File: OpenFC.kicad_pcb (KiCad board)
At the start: 8 copper layers, 29.5 x 27.6 mm, 173 parts, among them J1 5V, J13 5V, J14 5V, J15 5V, J16 5V, J17 5V, J18 5V, J19 5V, J2 5V, J20 5V, J21 5V, J22 5V, J23 5V, J24 5V, J25 5V, J26 5V, J27 5V, J28 5V, J29 5V, J3 5V, J30 5V, J31 5V, J32 5V, J33 5V, J34 5V, J35 5V, J36 5V, J37 5V, J38 5V, J39 5V, J4 5V, J40 5V, J41 5V, J42 5V, J43 5V, J44 5V, J45 5V, J46 5V, J47 5V, J48 5V, J5 5V, J53 5V, J57 5V, J59 5V, J6 5V, J7 5V, J8 5V, J9 5V, P1 SM08B-SRSS-TB(LF)(SN), Q7 DMN1150UFB-7B, U1 SM06B-SRSS-TB(LF)(SN), U10 TLV75533PDBVR, U11 RP2350A_C42411118, U12 ABM8-272-T3_C20625731, U13 W25Q32RVXHJQ TR, U14 LSM6DSV16XTR, U15 XL-1010RGBC-WS2812B, U16 XL-1010RGBC-WS2812B, U17 XL-1010RGBC-WS2812B, U18 XL-1010RGBC-WS2812B, U19 ESP8285H16, U2 W25Q128JVPIQTR, U20 SX1281IMLTRT, U21 TS2306A 240GF MSM 9_C2976675, U22 XL-1010RGBC-WS2812B, U23 XL-1010RGBC-WS2812B, U24 XL-1010RGBC-WS2812B, U25 XL-1010RGBC-WS2812B, U26 XL-1010RGBC-WS2812B, U27 XL-1010RGBC-WS2812B, U28 XL-1010RGBC-WS2812B, U29 XL-1010RGBC-WS2812B, U3 XL-1010RGBC-WS2812B, U30 BMP388, U4 XL-1010RGBC-WS2812B, U5 XL-1010RGBC-WS2812B, U6 LMR51420YDDCR, U7 LMR51420YDDCR, U8 XL-1010RGBC-WS2812B, U9 TLV75533PDBVR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

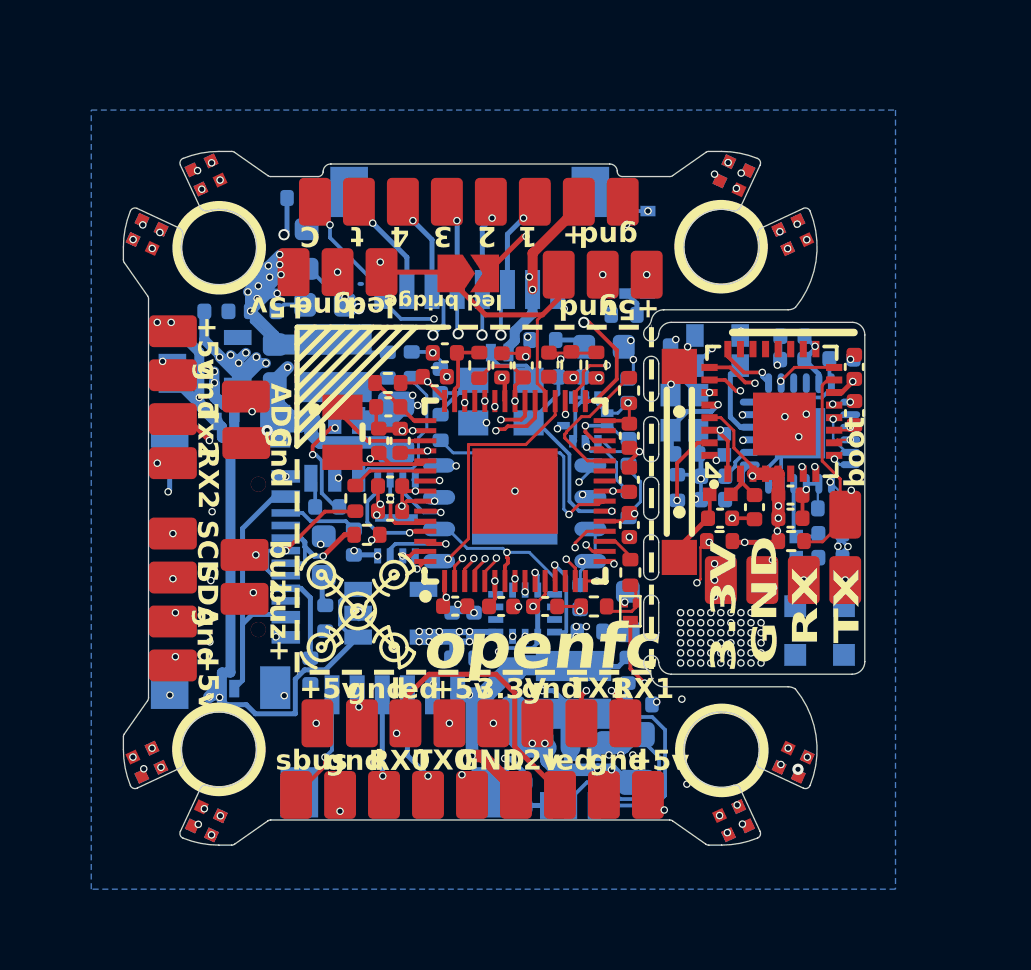
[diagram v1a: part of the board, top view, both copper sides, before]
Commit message: Switched to RP2354A and re-routed
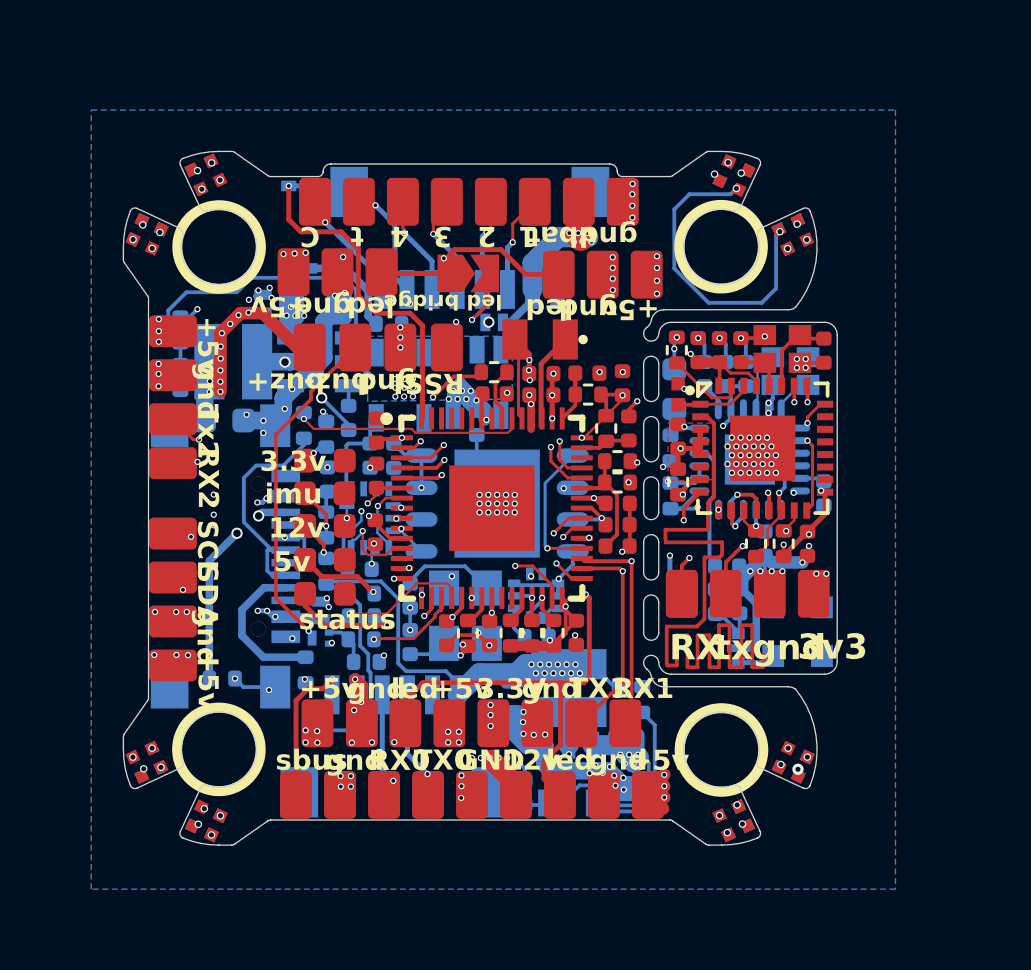
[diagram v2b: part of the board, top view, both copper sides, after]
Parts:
- removed C10, C100, C101, C102, C103, C104, C109, C46, C47, C48, C97, C98, C99: 100n, Capacitor_SMD:C_0402_1005Metric
- removed C105, C106: 15p, Capacitor_SMD:C_0402_1005Metric
- removed C43, C44, C45: 4.7uF, Capacitor_SMD:C_0402_1005Metric
- removed D2: LED_1_Green, LED_SMD:LED_0603_1608Metric
- removed J57: 5V, lib:small_pad
- removed L13: ANT8010LL04R2400A, lib:ANT-SMD_L8.0-W1.0-SLDA81-3R010G-S1TF
- removed L7, L9: LQW15AN3N0B00D (3nH), lib:L0402
- removed OSC1: OW7EL89CENUNFAYLC-52M, lib:OSC-SMD_4P-L2.0-W1.6-BL_TXC_7Z
- removed R1, R2: 5.1k, Resistor_SMD:R_0402_1005Metric
- removed R10, R12: 10k, Resistor_SMD:R_0402_1005Metric
- removed R39: 33R, Resistor_SMD:R_0402_1005Metric
- removed R41: 200R, Resistor_SMD:R_0402_1005Metric
- removed R42: 1k, Resistor_SMD:R_0402_1005Metric
- removed R46, R47: 22R, Resistor_SMD:R_0402_1005Metric
- removed R53: 30R, Resistor_SMD:R_0402_1005Metric
- removed U11: RP2350A_C42411118, lib:QFN-60_L7.0-W7.0-P0.40-TL-EP3.4
- removed U12: ABM8-272-T3_C20625731, lib:CRYSTAL-SMD_4P-L3.2-W2.5-BL
- removed U13: W25Q32RVXHJQ TR, lib:USON-8_L3.0-W2.0-P0.50-BL-EP
- removed U21: TS2306A 240GF MSM 9_C2976675, lib:SW-SMD_4P-L3.0-W2.0-P0.85-LS3.5
- added C21: 4.7uF, Capacitor_SMD:C_0402_1005Metric, F.Cu at (65.9, 106.5)
- added C22: 4.7uF, Capacitor_SMD:C_0402_1005Metric, F.Cu at (67.7, 106.5)
- added C23: 4.7uF, Capacitor_SMD:C_0402_1005Metric, F.Cu at (69.4, 108.7)
- added C24: 100n, Capacitor_SMD:C_0402_1005Metric, F.Cu at (76.5, 113.3)
- added C25: 100n, Capacitor_SMD:C_0402_1005Metric, F.Cu at (68.9, 112.5)
- added C26: 100n, Capacitor_SMD:C_0402_1005Metric, F.Cu at (69.1, 106.9)
- added C27: 100n, Capacitor_SMD:C_0402_1005Metric, F.Cu at (64.0, 107.3)
- added C28: 100n, Capacitor_SMD:C_0402_1005Metric, F.Cu at (67.3, 116.8)
- added C29: 100n, Capacitor_SMD:C_0402_1005Metric, F.Cu at (59.3, 112.8)
- added C30: 100n, Capacitor_SMD:C_0402_1005Metric, F.Cu at (62.1, 116.8)
- added C31: 100n, Capacitor_SMD:C_0402_1005Metric, F.Cu at (59.4, 108.8)
- added C32: 15p, Capacitor_SMD:C_0402_1005Metric, B.Cu at (60.7, 117.2)
- added C33: 15p, Capacitor_SMD:C_0402_1005Metric, B.Cu at (60.7, 115.3)
- added C34: 100n, Capacitor_SMD:C_0402_1005Metric, B.Cu at (58.7, 114.3)
- added C6: 4.7uF, Capacitor_SMD:C_0402_1005Metric, F.Cu at (65.9, 107.3)
- added D6: LED_1_Green, LED_SMD:LED_0603_1608Metric, F.Cu at (57.3, 115.2)
- added D7: LED, LED_SMD:LED_0603_1608Metric, B.Cu at (71.2, 107.1)
- added FL1: 2450FM07D0034T, lib:FILTER-SMD_4P-L1.0-W0.5-L, B.Cu at (73.8, 117.4)
- added J56: 5V, lib:small_pad, F.Cu at (62.1, 105.5)
- added L2: AOTA-B201610S3R3-101-T, lib:IND-SMD_L2.0-W1.6_AOTA-B201610S3R3-101-T, F.Cu at (65.9, 105.1)
- added R17: 22R, Resistor_SMD:R_0402_1005Metric, B.Cu at (56.5, 108.5)
- added R18: 22R, Resistor_SMD:R_0402_1005Metric, F.Cu at (64.0, 106.4)
- added R19: 33R, Resistor_SMD:R_0402_1005Metric, F.Cu at (67.8, 107.3)
- added R20: 200R, Resistor_SMD:R_0402_1005Metric, F.Cu at (68.5, 108.7)
- added R21: 1k, Resistor_SMD:R_0402_1005Metric, F.Cu at (63.0, 116.8)
- added R22: 30R, Resistor_SMD:R_0402_1005Metric, B.Cu at (58.8, 116.1)
- added R23: 5.1k, Resistor_SMD:R_0402_1005Metric, F.Cu at (65.5, 116.8)
- added R24: 5.1k, Resistor_SMD:R_0402_1005Metric, F.Cu at (66.4, 116.8)
- added R25: 10k, Resistor_SMD:R_0402_1005Metric, F.Cu at (64.7, 116.8)
- added R26: 10k, Resistor_SMD:R_0402_1005Metric, B.Cu at (59.8, 104.5)
- added R33: 3.3k, Resistor_SMD:R_0402_1005Metric, B.Cu at (71.0, 109.5)
- added R35: 10k, Resistor_SMD:R_0402_1005Metric, F.Cu at (74.5, 113.3)
- added U32: RP2354A, lib:QFN-60_L7.0-W7.0-P0.40-TL-EP3.4, F.Cu at (63.9, 111.8)
- added U33: ABM8-272-T3_C20625731, lib:CRYSTAL-SMD_4P-L3.2-W2.5-BL, B.Cu at (62.9, 116.1)
- added U34: TS2306A 240GF MSM 9_C2976675, lib:SW-SMD_4P-L3.0-W2.0-P0.85-LS3.5, B.Cu at (56.3, 100.7)
- added X2: Q22FA12800519, lib:CRYSTAL-SMD_4P-L2.0-W1.6-BL, B.Cu at (75.8, 106.4)
- C13, C18, C19, D1, D3, D4, D5, L8, R7, X1: moved to F.Cu
- C14, C8, J59, Q7, R13, R5: moved to B.Cu
- C15: value 1.2p -> 100n
- C20: value 1.2p -> 100n; moved to F.Cu
- C42: value 4.7uF -> 100n
- L1: value AOTA-B201610S3R3-101-T -> 3n; footprint lib:IND-SMD_L2.0-W1.6_AOTA-B201610S3R3-101-T -> Inductor_SMD:L_0402_1005Metric; moved to B.Cu
- moved L1 16.3 mm to (72.8, 115.5), turned to -90 degrees
- moved C20 13.9 mm to (63.9, 116.8), turned to -90 degrees
- moved C15 13.8 mm to (59.4, 110.5), turned to 90 degrees
- moved D4 12.9 mm to (57.3, 111.2), turned to 180 degrees
- moved Q7 12.4 mm to (57.1, 117.0), turned to 0 degrees
- moved R15 11.9 mm to (58.8, 115.2)
- moved R4 11.3 mm to (57.4, 112.5), turned to -90 degrees
- moved C3 11.3 mm to (63.3, 108.5), turned to -90 degrees
- moved R13 11.0 mm to (58.7, 117.1), turned to 180 degrees
- moved U9 10.9 mm to (63.4, 106.8), turned to 90 degrees
- moved C111 10.4 mm to (65.7, 117.0), turned to 180 degrees
- moved J39 10.3 mm to (56.7, 105.5), turned to 90 degrees
- moved D1 10.2 mm to (57.3, 113.9)
- moved C42 9.83 mm to (69.0, 111.7), turned to 0 degrees
- moved R3 9.46 mm to (57.4, 108.9), turned to -90 degrees
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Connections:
- net /RP2350A/VBAT_ADC renamed Net-(U32-GPIO26_ADC0)
- AE1 pad 3: Net-(AE1-Pad3) -> Net-(FL1-OUT)
- C14 pad 1: Net-(U19-LNA) -> Net-(U20-RFIO)
- C15 pad 1: Net-(C15-Pad1) -> +1.1V
- C17 pad 1: Net-(U20-RFIO) -> Net-(FL1-IN)
- C20 pad 1: Net-(AE1-Pad3) -> +1.1V
- L1 pad 1: +1.1V -> Net-(U20-RFIO)
- L1 pad 2: Net-(U11-VREG_LX) -> Net-(FL1-IN)
- U14 pad 2: unconnected-(U14-SDx/AH1/Qvar1-Pad2) -> GND
- U14 pad 3: unconnected-(U14-SCx/AH2/Qvar2-Pad3) -> GND
- U19 pad 14: +3.3V -> /ELRS/RST
- U19 pad 2: Net-(U19-LNA) -> /ELRS/ANT_TRACE
- U19 pad 8: /ELRS/RST -> Net-(U19-XDP_DCDC)
- U20 pad 4: /ELRS/RADIO_OSC -> Net-(U20-XTA)
- U20 pad 6: unconnected-(U20-XTB-Pad6) -> Net-(U20-XTB)
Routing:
- net +4.5V: track 135.7 -> 36.6 mm, vias 11 -> 28
- net /ELRS/ANT_TRACE: track 0.00 -> 32.7 mm
- net Net-(U11-QSPI_SS): track 30.0 -> 0.00 mm, vias 2 -> 0
- net +3.3V: track 80.7 -> 56.0 mm
- net GND: track 82.1 -> 65.2 mm, vias 138 -> 154
- net /PADS/BUZZER-: track 29.2 -> 13.5 mm, vias 2 -> 1
- net Net-(U32-QSPI_SS): track 0.00 -> 14.0 mm, vias 0 -> 1
- net /PADS/SBUS: track 4.57 -> 17.5 mm, vias 1 -> 2
- net /ELRS/ESP_BOOT0: track 33.0 -> 20.6 mm, vias 2 -> 3
- net /PADS/CURRENT: track 10.5 -> 22.1 mm, vias 3 -> 2
- net +5V: track 38.0 -> 27.3 mm, vias 20 -> 35
- net /PADS/ADC1: track 9.96 -> 0.00 mm, vias 2 -> 0
- net Net-(U11-XOUT): track 9.20 -> 0.00 mm, vias 1 -> 0
- net Net-(U32-USB_DM): track 0.00 -> 8.99 mm, vias 0 -> 1
- net /PADS/ADC2: track 0.00 -> 8.64 mm, vias 0 -> 2
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- added copper zone on F.Cu, net +3.3V
- added copper zone on B.Cu, net +4.5V
- added copper zone on In5.Cu, net +4.5V
- removed copper zone on In4.Cu, net +3.3V_GYRO
- removed copper zone on In5.Cu, net GND
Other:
- board size 29.5 x 27.6 mm -> 28.4 x 27.6 mm
- board text added: "3.3v"
- board text added: "3v3"
- board text added: "5v"
- board text added: "RSSI"
- board text added: "imu"
- board text added: "tx"
- board text added: "vbat"
- board text removed: "+"
- board text removed: "+12v"
- board text removed: "+3.3 imu"
- board text removed: "+3.3v"
- board text removed: "ADC"
- board text removed: "EXPRESSLRS"
- board text removed: "TX"
- board text removed: "break me"
- board text removed: "receiver"

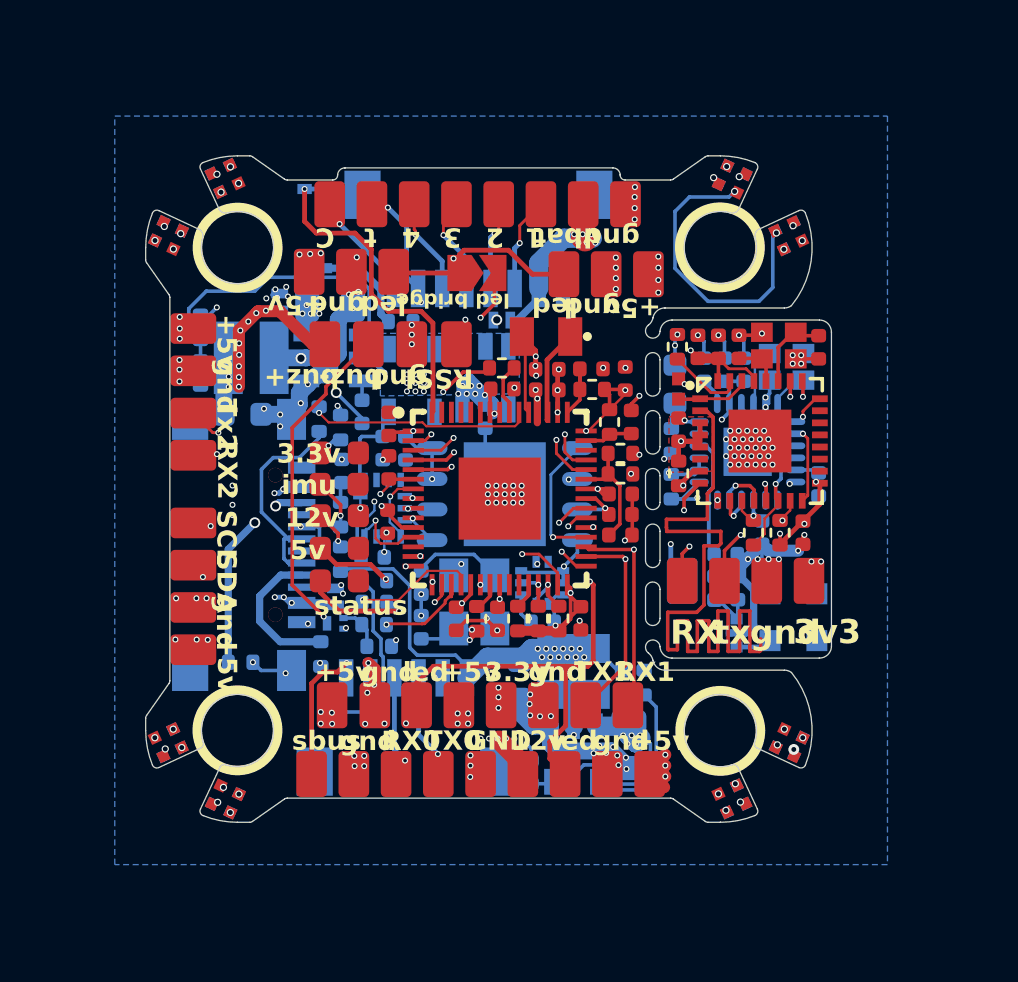
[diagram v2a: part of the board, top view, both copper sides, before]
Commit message: Added Open-OSD-X and new layout
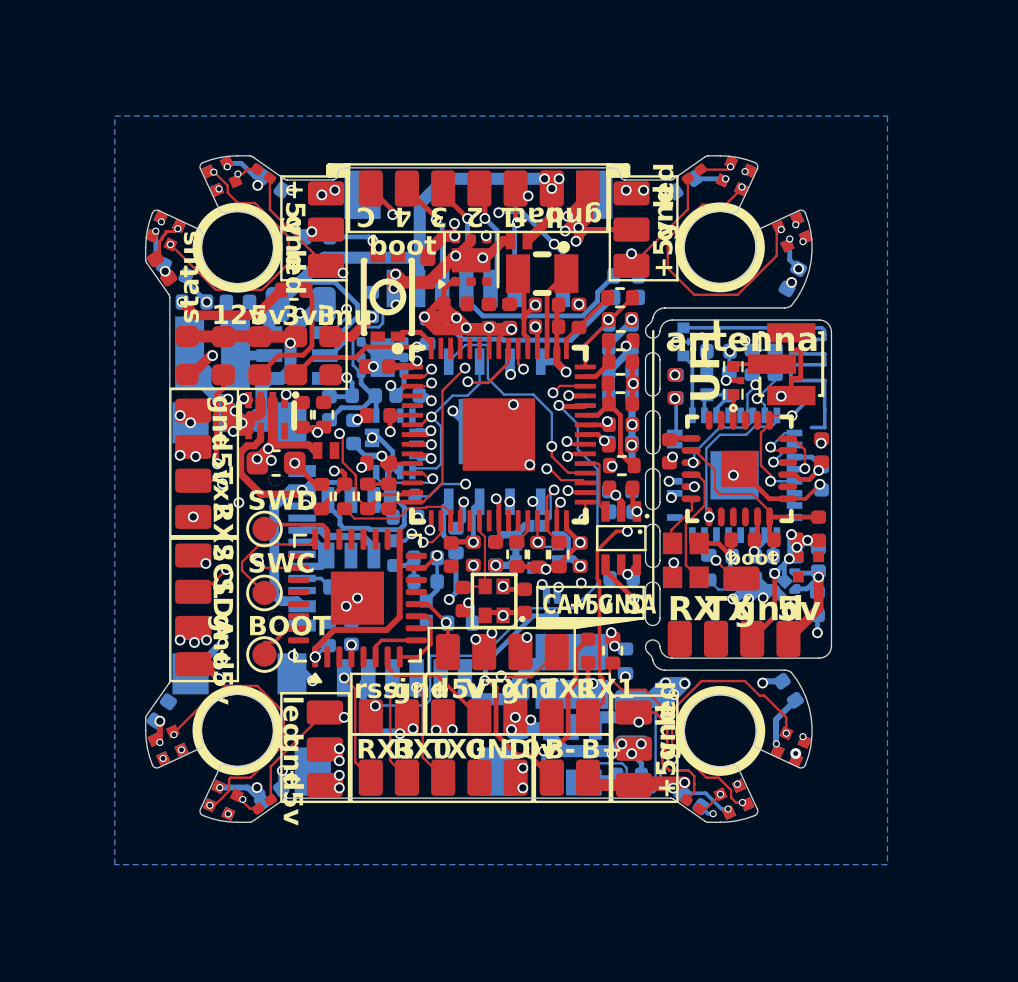
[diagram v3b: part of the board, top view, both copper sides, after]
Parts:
- removed AE1: 47948-0001, lib:ANT-SMD_47948-0001
- removed C110: 100n, Capacitor_SMD:C_0402_1005Metric
- removed D20, D23: RB161QS-40_C28646385, lib:SOD-882_L1.0-W0.6-RD
- removed D7: LED, LED_SMD:LED_0603_1608Metric
- removed J37, J41, J59: 5V, lib:small_pad
- removed L8: BLM15PD121SN1D, lib:L0402
- removed R33: 3.3k, Resistor_SMD:R_0402_1005Metric
- removed R35: 10k, Resistor_SMD:R_0402_1005Metric
- removed X1: XTM20026000FT00351005, lib:CRYSTAL-SMD_4P-L2.0-W1.6-BL
- added C10: 100n, Capacitor_SMD:C_0402_1005Metric, F.Cu at (65.0, 116.1)
- added C16: 22uF, Capacitor_SMD:C_0402_1005Metric, F.Cu at (62.1, 103.8)
- added C43: 22uF, Capacitor_SMD:C_0402_1005Metric, B.Cu at (56.9, 108.1)
- added C44: 100n, Capacitor_SMD:C_0402_1005Metric, B.Cu at (69.0, 115.2)
- added C45: 100n, Capacitor_SMD:C_0402_1005Metric, F.Cu at (61.9, 114.2)
- added C46: 100n, Capacitor_SMD:C_0402_1005Metric, B.Cu at (54.5, 124.1)
- added C47: 100n, Capacitor_SMD:C_0402_1005Metric, B.Cu at (50.0, 120.7)
- added C48: 22uF, Capacitor_SMD:C_0603_1608Metric, F.Cu at (54.7, 110.4)
- added C49: 100n, Capacitor_SMD:C_0402_1005Metric, B.Cu at (68.9, 111.5)
- added C50: 100n, Capacitor_SMD:C_0402_1005Metric, B.Cu at (73.5, 107.1)
- added C51: 100n, Capacitor_SMD:C_0402_1005Metric, B.Cu at (73.0, 105.7)
- added C52: 100n, Capacitor_SMD:C_0402_1005Metric, B.Cu at (71.2, 107.2)
- added C53: 100n, Capacitor_SMD:C_0402_1005Metric, B.Cu at (74.0, 114.2)
- added C54: 100n, Capacitor_SMD:C_0402_1005Metric, B.Cu at (77.3, 111.0)
- added C55: 100n, Capacitor_SMD:C_0402_1005Metric, B.Cu at (75.8, 114.2)
- added C56: 100n, Capacitor_SMD:C_0402_1005Metric, F.Cu at (71.2, 107.2)
- added C57: 100n, Capacitor_SMD:C_0402_1005Metric, B.Cu at (75.9, 119.8)
- added C58: 100n, Capacitor_SMD:C_0402_1005Metric, B.Cu at (71.9, 124.3)
- added C59: 100n, Capacitor_SMD:C_0402_1005Metric, B.Cu at (68.9, 109.5)
- added C60: 100n, Capacitor_SMD:C_0402_1005Metric, B.Cu at (68.9, 107.6)
- added C61: 100n, Capacitor_SMD:C_0402_1005Metric, B.Cu at (68.9, 105.6)
- added C64: 100n, Capacitor_SMD:C_0402_1005Metric, B.Cu at (68.9, 106.6)
- added C65: 100n, Capacitor_SMD:C_0402_1005Metric, B.Cu at (68.9, 104.6)
- added C66: 100n, Capacitor_SMD:C_0402_1005Metric, B.Cu at (69.0, 112.4)
- added C69: 100n, Capacitor_SMD:C_0402_1005Metric, B.Cu at (60.9, 114.3)
- added C71: 100n, Capacitor_SMD:C_0402_1005Metric, B.Cu at (60.9, 115.3)
- added C75: 100n, Capacitor_SMD:C_0402_1005Metric, B.Cu at (56.9, 117.5)
- added C76: 100n, Capacitor_SMD:C_0402_1005Metric, B.Cu at (57.8, 117.4)
- added D2: USBLC6-2SC6, lib:SOT-23-6_L2.9-W1.6-P0.95-LS2.8-BL, B.Cu at (57.8, 113.0)
- added D8: LED_1_Green, LED_SMD:LED_0603_1608Metric, F.Cu at (56.9, 105.9)
- added FL2: 2450FM07D0034T, lib:FILTER-SMD_4P-L1.0-W0.5-L, B.Cu at (71.5, 105.3)
- added J10: 5V, lib:small_pad, F.Cu at (72.9, 117.7)
- added J11: 5V, lib:small_pad, F.Cu at (71.4, 117.7)
- added J12: 5V, lib:small_pad, F.Cu at (74.0, 115.2)
- added J49: 5V, lib:small_pad, F.Cu at (63.3, 118.2)
- added J50: 5V, lib:small_pad, F.Cu at (64.8, 118.2)
- added JP2: SolderJumper_2_Open, Panelization:MouseBite-Slot-Jumper_0201, F.Cu at (71.9, 124.5)
- added JP3: SolderJumper_2_Open, Panelization:MouseBite-Slot-Jumper_0201, F.Cu at (54.2, 98.4)
- added JP4: SolderJumper_2_Open, Panelization:MouseBite-Slot-Jumper_0201, F.Cu at (72.0, 98.4)
- added L7: LQG15HS2N0S02D, lib:L0402, B.Cu at (72.5, 107.1)
- added R1: 10k, Resistor_SMD:R_0402_1005Metric, B.Cu at (72.6, 114.7)
- added R10: 6.8k, Resistor_SMD:R_0402_1005Metric, F.Cu at (59.4, 111.8)
- added R2: 75, Resistor_SMD:R_0402_1005Metric, B.Cu at (62.3, 117.0)
- added R34: 6.8k, Resistor_SMD:R_0402_1005Metric, F.Cu at (58.5, 111.8)
- added R36: 6.8k, Resistor_SMD:R_0402_1005Metric, B.Cu at (69.2, 102.6)
- added R37: 6.8k, Resistor_SMD:R_0402_1005Metric, B.Cu at (69.2, 103.5)
- added RF1: CONUFL001-SMD-T, lib:IPEX-SMD_3P-L2.6-W2.6-LS3.0, F.Cu at (75.6, 106.3)
- added TP1: TestPoint, TestPoint:TestPoint_Pad_D1.0mm, F.Cu at (54.2, 113.1)
- added TP2: TestPoint, TestPoint:TestPoint_Pad_D1.0mm, F.Cu at (54.2, 115.8)
- added TP3: TestPoint, TestPoint:TestPoint_Pad_D1.0mm, F.Cu at (54.2, 118.3)
- added U12: WL9005D4-33, lib:UDFN-4_L1.0-W1.0-P0.65-TL, B.Cu at (75.8, 115.3)
- added U13: TPS746-3.3DRV, Package_SON:WSON-6-1EP_2x2mm_P0.65mm_EP1x1.6mm, F.Cu at (62.8, 102.0)
- added U21: TPS746-3.3DRV, Package_SON:WSON-6-1EP_2x2mm_P0.65mm_EP1x1.6mm, B.Cu at (59.1, 106.0)
- added U35: STM32G431KBUx, Package_DFN_QFN:QFN-32-1EP_5x5mm_P0.5mm_EP3.1x3.1mm, F.Cu at (58.0, 116.0)
- added X3: OT4EL89CJI-111YLC-12M, lib:OSC-SMD_4P-L1.6-W1.2-BL-1, F.Cu at (63.7, 116.1)
- C1, C36, C5, C7, C8, C9, D21, FL1, R13, R14, R15, R5, U20, U34, X2: moved to F.Cu
- C11, C12, C13, R18, R6: moved to B.Cu
- C14: value 1.2p -> 100n
- C17: value 1.2p -> 22uF
- C18: value 15p -> 100n; moved to B.Cu
- C19, C33: value 15p -> 100n
- C3: value 22uF -> 15p; moved to F.Cu
- C32: value 15p -> 100n; moved to F.Cu
- C4: value 22uF -> 100n; moved to F.Cu
- D3: value LED_1_Green -> RB161QS-40_C28646385; footprint LED_SMD:LED_0603_1608Metric -> lib:SOD-882_L1.0-W0.6-RD
- JP1: footprint Jumper:SolderJumper-2_P1.3mm_Open_TrianglePad1.0x1.5mm -> Panelization:MouseBite-Slot-Jumper_0201
- L1: value 3n -> BLM15AG601SN1D; footprint Inductor_SMD:L_0402_1005Metric -> lib:L0402
- R21: value 1k -> 33R; moved to B.Cu
- R3: value 33R -> 10k
- R7: value 12k -> 100k
- R8: value 10k -> 39k
- U10: value TLV75533PDBVR -> GD25Q256EWIGR; footprint lib:SOT-23-5_L3.0-W1.7-P0.95-LS2.8-BR -> lib:WSON-8_L6.0-W5.0-P1.27-TL-EP
- U19: value ESP8285H16 -> XL-1010RGBC-WS2812B; footprint lib:QFN-32_L5.0-W5.0-P0.50-TL-EP3.7 -> lib:LED-SMD_4P-L1.0-W1.0-TL_XL-1010RGBC-WS2812B
- U2: value W25Q128JVPIQTR -> ESP32-C3FH4; footprint lib:WSON-8_L6.0-W5.0-P1.27-BL-EP -> lib:QFN-32_L5.0-W5.0-P0.50-TL-EP3.7
- U33: value ABM8-272-T3_C20625731 -> TPS2116DRLR; footprint lib:CRYSTAL-SMD_4P-L3.2-W2.5-BL -> lib:SOT-583-8_L2.1-W1.6-P0.50-LS1.6-BL; moved to F.Cu
- U9: value TLV75533PDBVR -> TXU0101DCKR; footprint lib:SOT-23-5_L3.0-W1.7-P0.95-LS2.8-BR -> lib:SC-70-6_L2.0-W1.3-P0.65-LS2.1-BL; moved to F.Cu
- moved J26 24.9 mm to (75.9, 117.7)
- moved C19 24.1 mm to (50.0, 102.3), turned to -55 degrees
- moved JP1 23.7 mm to (54.2, 124.5), turned to -55 degrees
- moved C18 23.6 mm to (54.5, 98.8), turned to -35 degrees
- moved J39 21.0 mm to (67.6, 123.4)
- moved R8 19.5 mm to (56.6, 108.4)
- moved J40 19.5 mm to (66.1, 123.4)
- moved R3 18.2 mm to (75.3, 106.2)
- moved J56 15.9 mm to (58.6, 120.9)
- moved R7 15.8 mm to (55.8, 108.4), turned to -90 degrees
- moved J9 15.5 mm to (60.1, 120.9)
- moved C32 14.8 mm to (61.0, 102.4)
- moved R21 13.7 mm to (58.6, 103.8), turned to -90 degrees
- moved C28 12.9 mm to (64.3, 104.3), turned to 90 degrees
- moved R29 12.5 mm to (69.2, 118.6), turned to -90 degrees
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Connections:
- net /PADS/M1 renamed /RP2350A/Motor1
- net /PADS/M2 renamed /RP2350A/Motor2
- net /PADS/M3 renamed /RP2350A/Motor3
- net /PADS/M4 renamed /RP2350A/Motor4
- C11 pad 1: +3.3V -> +5V
- C12 pad 1: +3.3V -> +5V
- C13 pad 1: +3.3V -> +5V
- C14 pad 1: Net-(U20-RFIO) -> +5V
- C17 pad 1: Net-(FL1-IN) -> +3.3V_ELRS
- C18 pad 1: GND -> +5V
- C18 pad 2: Net-(U19-XTAL_OUT) -> GND
- C19 pad 1: GND -> +5V
- C19 pad 2: Net-(U19-XTAL_IN) -> GND
- C3 pad 1: +3.3V -> GND
- C3 pad 2: GND -> /RP2350A/Xin
- C32 pad 1: GND -> +5V
- C32 pad 2: Net-(C32-Pad2) -> GND
- C33 pad 1: /RP2350A/Xin -> +5V
- C4 pad 1: +3.3V_GYRO -> +3.3V
- C40 pad 1: +5V -> +5V_BUCK
- C5 pad 1: +3.3V -> +3.3V_ELRS
- C8 pad 1: +3.3V -> +3.3V_ELRS
- D3 pad 1: GND -> +5V
- D3 pad 2: Net-(D3-A) -> +5V_BUCK
- J26 pad 1: /PADS/ESC_TELEM -> +5V
- J31 pad 1: +3.3V -> GND
- J32 pad 1: /UART1_RX -> /OSD/VIDEO_IN
- J33 pad 1: /UART1_TX -> /OSD/VIDEO_OUT
- J34 pad 1: GND -> /OSD/SA_OUT
- L1 pad 1: Net-(U20-RFIO) -> +3.3V
- L1 pad 2: Net-(FL1-IN) -> Net-(U35-VDDA)
- L4 pad 2: +5V -> +5V_BUCK
- P1 pad 1: /PADS/CURRENT -> GND
- P1 pad 2: /PADS/ESC_TELEM -> +BATT
- P1 pad 8: GND -> /PADS/CURRENT
- R15 pad 1: +5V -> +5V_BUCK
- R16 pad 2: +5V -> +5V_BUCK
- R21 pad 1: Net-(C32-Pad2) -> +3.3V_GYRO
- R21 pad 2: /RP2350A/Xout -> Net-(D8-A)
- R3 pad 1: +3.3V -> +3.3V_ELRS
- R3 pad 2: Net-(D3-A) -> /ELRS/ESP8285_EN
- R4 pad 1: +3.3V_GYRO -> +3.3V
- R6 pad 1: +3.3V -> +3.3V_ELRS
- R6 pad 2: /ELRS/ESP8285_EN -> /ELRS/RST
- R7 pad 1: Net-(U19-RES12K) -> +5V_BUCK
- R7 pad 2: GND -> Net-(U33-PR1)
- R8 pad 1: +3.3V -> Net-(U33-PR1)
- R8 pad 2: /ELRS/ESP_BOOT0 -> GND
- U10 pad 1: +4.5V -> /BLACKBOX/BB_CS
- U10 pad 2: GND -> /BLACKBOX/SPI.MISO
- U10 pad 3: +4.5V -> +3.3V
- U10 pad 4: unconnected-(U10-NC-Pad4) -> GND
- U10 pad 5: +3.3V_GYRO -> /BLACKBOX/SPI.MOSI
- U15 pad 2: +4.5V -> +5V
- U15 pad 4: Net-(U15-DIN) -> Net-(JP1-B)
- U16 pad 2: +4.5V -> +5V
- U17 pad 2: +4.5V -> +5V
- U17 pad 4: Net-(U16-DOUT) -> Net-(JP2-B)
- U18 pad 2: +4.5V -> +5V
- U19 pad 1: Net-(L8-Pad2) -> unconnected-(U19-DOUT-Pad1)
- U19 pad 2: /ELRS/ANT_TRACE -> +5V
- U19 pad 3: +3.3V -> GND
- U19 pad 4: +3.3V -> /ELRS/RGBLED
- U2 pad 1: /BLACKBOX/BB_CS -> Net-(FL2-IN)
- U2 pad 2: /BLACKBOX/SPI.MISO -> Net-(C50-Pad1)
- U2 pad 3: +3.3V -> Net-(C50-Pad1)
- U2 pad 4: GND -> unconnected-(U2-XTAL_32K_P-Pad4)
- U2 pad 5: /BLACKBOX/SPI.MOSI -> unconnected-(U2-XTAL_32K_N-Pad5)
- U2 pad 6: /BLACKBOX/SPI.SCK -> /ELRS/RST
- U2 pad 7: +3.3V -> /ELRS/ESP8285_EN
- U2 pad 8: +3.3V -> /ELRS/BUSY
- U2 pad 9: GND -> /ELRS/MOSI
- U20 pad 11: +3.3V -> +3.3V_ELRS
- U20 pad 15: +3.3V -> +3.3V_ELRS
- U20 pad 22: Net-(U20-RFIO) -> Net-(FL1-IN)
- U22 pad 2: +4.5V -> +5V
- U23 pad 2: +4.5V -> +5V
- U24 pad 2: +4.5V -> +5V
- U25 pad 2: +4.5V -> +5V
- U25 pad 4: Net-(U15-DIN) -> Net-(U25-DIN)
- U26 pad 2: +4.5V -> +5V
- U27 pad 2: +4.5V -> +5V
- U28 pad 2: +4.5V -> +5V
- U29 pad 2: +4.5V -> +5V
- U3 pad 2: +4.5V -> +5V
- U3 pad 4: Net-(JP1-B) -> Net-(JP4-B)
- U32 pad 13: unconnected-(U32-GPIO9-Pad13) -> /OSD/OSD_RX
- U32 pad 22: /RP2350A/Xout -> unconnected-(U32-XOUT-Pad22)
- U32 pad 31: /PADS/ESC_TELEM -> /RP2350A/UART3_RX
- U32 pad 35: /LED -> /RP2350A/LED_STRIP_L
- U32 pad 43: unconnected-(U32-GPIO29_ADC3-Pad43) -> /OSD/OSD_TX
- U33 pad 1: /RP2350A/Xin -> GND
- U33 pad 2: GND -> +5V
- U33 pad 3: Net-(C32-Pad2) -> +5V_BUCK
- U33 pad 4: GND -> Net-(U33-PR1)
- U4 pad 2: +4.5V -> +5V
- U5 pad 2: +4.5V -> +5V
- U5 pad 4: Net-(U23-DIN) -> Net-(JP3-B)
- U8 pad 1: Net-(U15-DIN) -> Net-(U25-DIN)
- U8 pad 2: +4.5V -> +5V
- U9 pad 1: +4.5V -> +3.3V
- U9 pad 3: +4.5V -> /RP2350A/LED_STRIP_L
- U9 pad 4: unconnected-(U9-NC-Pad4) -> /LED
- U9 pad 5: +3.3V -> +5V
- USB2 pad A6: /RP2350A/D+ -> /RP2350A/D+_C
- USB2 pad A7: /RP2350A/D- -> /RP2350A/D-_C
- USB2 pad B6: /RP2350A/D+ -> /RP2350A/D+_C
- USB2 pad B7: /RP2350A/D- -> /RP2350A/D-_C
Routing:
- net GND: track 65.2 -> 124.4 mm, vias 154 -> 91
- net +5V: track 27.3 -> 64.3 mm, vias 35 -> 37
- net +4.5V: track 36.6 -> 0.00 mm, vias 28 -> 0
- net Net-(D5-A): track 1.64 -> 33.5 mm, vias 1 -> 2
- net /LED: track 41.6 -> 70.3 mm, vias 4 -> 5
- net +5V_BUCK: track 0.00 -> 24.2 mm, vias 0 -> 5
- net Net-(D6-A): track 4.72 -> 28.7 mm, vias 1 -> 2
- net Net-(U23-DIN): track 22.3 -> 0.00 mm, vias 2 -> 1
- net Net-(U15-DIN): track 22.2 -> 0.00 mm, vias 2 -> 0
- net Net-(U16-DOUT): track 20.8 -> 0.00 mm, vias 2 -> 1
- net /ELRS/ESP_BOOT0: track 20.6 -> 1.36 mm, vias 3 -> 1
- net /PADS/ESC_TELEM: track 18.4 -> 0.00 mm, vias 3 -> 0
- net +12V: track 26.6 -> 9.12 mm, vias 17 -> 4
- net +3.3V_ELRS: track 0.00 -> 17.0 mm, vias 0 -> 9
- net /ELRS/ANT_TRACE: track 32.7 -> 16.1 mm
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- added copper zone on In5.Cu, net +5V
- removed copper zone on F.Cu, net +3.3V
- removed copper zone on B.Cu, net +4.5V
- removed copper zone on In5.Cu, net +4.5V
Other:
- board text added: "10v"
- board text added: "B+"
- board text added: "B-"
- board text added: "BOOT"
- board text added: "CAM"
- board text added: "ELRS"
- board text added: "RX3"
- board text added: "SA"
- board text added: "SWC"
- board text added: "SWD"
- board text added: "TX"
- board text added: "UFL"
- board text added: "VTX"
- board text added: "antenna"
- board text added: "bat"
- board text added: "break me"
- board text added: "rssi"
- board text removed: "3.3V"
- board text removed: "3.3v"
- board text removed: "Keep Out"
- board text removed: "RSSI"
- board text removed: "buz+"
- board text removed: "buz-"
- board text removed: "led bridge"
- board text removed: "openfc"
- board text removed: "sbus"
- board text removed: "t"
- board text removed: "tx"
- board text removed: "vbat"
